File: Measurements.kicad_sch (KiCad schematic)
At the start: 23 parts, among them U5 LMV324

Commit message: Первая версия в производство
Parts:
- added J12: Current Measure, Connector_Molex:Molex_Micro-Fit_3.0_43045-0400_2x02_P3.00mm_Horizontal, symbol Connector_Generic:Conn_02x02_Odd_Even
- added J6: Voltage measure, Connector_Molex:Molex_Micro-Fit_3.0_43045-0400_2x02_P3.00mm_Horizontal, symbol Connector_Generic:Conn_02x02_Odd_Even
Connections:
- net GND: now also J12.1 (Pin_1), J12.3 (Pin_3), J6.1 (Pin_1), J6.2 (Pin_2)
- net I_INDUCT: now also J12.2 (Pin_2), J12.4 (Pin_4)
- net V_IN: now also J6.3 (Pin_3)
- net V_OUT: now also J6.4 (Pin_4)
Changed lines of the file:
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@@
   (junction (at 133.985 68.58) (diameter 0) (color 0 0 0 0)
+  )
+  (junction (at 73.66 114.554) (diameter 0) (color 0 0 0 0)
   )
   (junction (at 144.145 68.58) (diameter 0) (color 0 0 0 0)
@@
   (no_connect (at 148.59 53.34))
   (no_connect (at 148.59 48.26))
+  (wire (pts (xy 72.39 112.014) (xy 73.66 112.014))
+    (stroke (width 0) (type default) (color 0 0 0 0))
+  )
   (wire (pts (xy 175.26 71.12) (xy 177.165 71.12))
     (stroke (width 0) (type default) (color 0 0 0 0))
@@
     (stroke (width 0) (type default) (color 0 0 0 0))
   )
+  (wire (pts (xy 56.896 112.014) (xy 56.896 114.554))
+    (stroke (width 0) (type default) (color 0 0 0 0))
+  )
   (wire (pts (xy 133.985 68.58) (xy 133.985 70.485))
     (stroke (width 0) (type default) (color 0 0 0 0))
   )
+  (wire (pts (xy 72.39 114.554) (xy 73.66 114.554))
+    (stroke (width 0) (type default) (color 0 0 0 0))
+  )
+  (wire (pts (xy 73.66 112.014) (xy 73.66 114.554))
+    (stroke (width 0) (type default) (color 0 0 0 0))
+  )
   (wire (pts (xy 211.455 95.885) (xy 211.455 96.52))
     (stroke (width 0) (type default) (color 0 0 0 0))
@@
     (stroke (width 0) (type default) (color 0 0 0 0))
   )
+  (wire (pts (xy 55.88 130.556) (xy 55.88 131.318))
+    (stroke (width 0) (type default) (color 0 0 0 0))
+  )
   (wire (pts (xy 143.51 100.33) (xy 143.51 99.695))
     (stroke (width 0) (type default) (color 0 0 0 0))
@@
     (stroke (width 0) (type default) (color 0 0 0 0))
   )
+  (wire (pts (xy 55.88 131.318) (xy 59.69 131.318))
+    (stroke (width 0) (type default) (color 0 0 0 0))
+  )
   (wire (pts (xy 133.985 68.58) (xy 135.89 68.58))
     (stroke (width 0) (type default) (color 0 0 0 0))
@@
     (stroke (width 0) (type default) (color 0 0 0 0))
   )
+  (wire (pts (xy 76.2 131.318) (xy 76.2 130.556))
+    (stroke (width 0) (type default) (color 0 0 0 0))
+  )
   (wire (pts (xy 143.51 117.475) (xy 143.51 118.745))
     (stroke (width 0) (type default) (color 0 0 0 0))
@@
     (stroke (width 0) (type default) (color 0 0 0 0))
   )
+  (wire (pts (xy 59.69 114.554) (xy 56.896 114.554))
+    (stroke (width 0) (type default) (color 0 0 0 0))
+  )
   (wire (pts (xy 140.97 68.58) (xy 144.145 68.58))
     (stroke (width 0) (type default) (color 0 0 0 0))
@@
     (stroke (width 0) (type default) (color 0 0 0 0))
   )
+  (wire (pts (xy 73.66 114.554) (xy 73.66 115.57))
+    (stroke (width 0) (type default) (color 0 0 0 0))
+  )
   (wire (pts (xy 143.51 124.46) (xy 143.51 123.825))
     (stroke (width 0) (type default) (color 0 0 0 0))
@@
     (stroke (width 0) (type default) (color 0 0 0 0))
   )
+  (wire (pts (xy 76.2 131.318) (xy 72.39 131.318))
+    (stroke (width 0) (type default) (color 0 0 0 0))
+  )
   (wire (pts (xy 127 120.015) (xy 127 124.46))
     (stroke (width 0) (type default) (color 0 0 0 0))
@@
     (stroke (width 0) (type default) (color 0 0 0 0))
   )
+  (wire (pts (xy 59.69 112.014) (xy 56.896 112.014))
+    (stroke (width 0) (type default) (color 0 0 0 0))
+  )
   (wire (pts (xy 174.625 120.015) (xy 176.53 120.015))
     (stroke (width 0) (type default) (color 0 0 0 0))
+  )
+  (global_label "V_OUT" (shape input) (at 72.39 133.858 0) (fields_autoplaced)
+    (effects (font (size 1.27 1.27)) (justify left))
+    (property "Intersheet References" "${INTERSHEET_REFS}" (id 0) (at 80.4879 133.9374 0)
+      (effects (font (size 1.27 1.27)) (justify left) hide)
+    )
   )
   (global_label "I_INDUCT" (shape input) (at 127 110.49 180) (fields_autoplaced)
@@
     )
   )
+  (global_label "V_IN" (shape input) (at 59.69 133.858 180) (fields_autoplaced)
+    (effects (font (size 1.27 1.27)) (justify right))
+    (property "Intersheet References" "${INTERSHEET_REFS}" (id 0) (at 53.2855 133.7786 0)
+      (effects (font (size 1.27 1.27)) (justify right) hide)
+    )
+  )
   (global_label "V_OUT_ADC" (shape input) (at 177.165 95.885 0) (fields_autoplaced)
     (effects (font (size 1.27 1.27)) (justify left))
@@
     (effects (font (size 1.27 1.27)) (justify right))
     (property "Intersheet References" "${INTERSHEET_REFS}" (id 0) (at 121.2305 61.5156 0)
+      (effects (font (size 1.27 1.27)) (justify right) hide)
+    )
+  )
+  (global_label "I_INDUCT" (shape input) (at 56.896 113.284 180) (fields_autoplaced)
+    (effects (font (size 1.27 1.27)) (justify right))
+    (property "Intersheet References" "${INTERSHEET_REFS}" (id 0) (at 46.1372 113.2046 0)
       (effects (font (size 1.27 1.27)) (justify right) hide)
     )
@@
     (pin "2")
   )
+  (symbol (lib_id "power:GND") (at 55.88 130.556 180) (unit 1)
+    (in_bom yes) (on_board yes)
+    (property "Reference" "#PWR027" (id 0) (at 55.88 124.206 0)
+      (effects (font (size 1.27 1.27)) hide)
+    )
+    (property "Value" "GND" (id 1) (at 55.88 127 0))
+    (property "Footprint" "" (id 2) (at 55.88 130.556 0)
+      (effects (font (size 1.27 1.27)) hide)
+    )
+    (property "Datasheet" "" (id 3) (at 55.88 130.556 0)
+      (effects (font (size 1.27 1.27)) hide)
+    )
+    (pin "1")
+  )
+  (symbol (lib_id "power:GND") (at 73.66 115.57 0) (unit 1)
+    (in_bom yes) (on_board yes)
+    (property "Reference" "#PWR028" (id 0) (at 73.66 121.92 0)
+      (effects (font (size 1.27 1.27)) hide)
+    )
+    (property "Value" "GND" (id 1) (at 75.438 119.126 0)
+      (effects (font (size 1.27 1.27)) (justify right))
+    )
+    (property "Footprint" "" (id 2) (at 73.66 115.57 0)
+      (effects (font (size 1.27 1.27)) hide)
+    )
+    (property "Datasheet" "" (id 3) (at 73.66 115.57 0)
+      (effects (font (size 1.27 1.27)) hide)
+    )
+    (pin "1")
+  )
   (symbol (lib_id "Device:R_Small") (at 133.35 97.79 180) (unit 1)
     (in_bom yes) (on_board yes)
@@
     )
     (pin "1")
+  )
+  (symbol (lib_id "Connector_Generic:Conn_02x02_Odd_Even") (at 67.31 114.554 180) (unit 1)
+    (in_bom yes) (on_board yes) (fields_autoplaced)
+    (property "Reference" "J12" (id 0) (at 66.04 105.41 0))
+    (property "Value" "Current Measure" (id 1) (at 66.04 107.95 0))
+    (property "Footprint" "Connector_Molex:Molex_Micro-Fit_3.0_43045-0400_2x02_P3.00mm_Horizontal" (id 2) (at 67.31 114.554 0)
+      (effects (font (size 1.27 1.27)) hide)
+    )
+    (property "Datasheet" "~" (id 3) (at 67.31 114.554 0)
+      (effects (font (size 1.27 1.27)) hide)
+    )
+    (pin "1")
+    (pin "2")
+    (pin "3")
+    (pin "4")
   )
   (symbol (lib_id "Device:R_Small") (at 167.005 120.015 270) (unit 1)
@@
     (pin "2")
   )
+  (symbol (lib_id "Connector_Generic:Conn_02x02_Odd_Even") (at 64.77 131.318 0) (unit 1)
+    (in_bom yes) (on_board yes) (fields_autoplaced)
+    (property "Reference" "J6" (id 0) (at 66.04 125.222 0))
+    (property "Value" "Voltage measure" (id 1) (at 66.04 127.762 0))
+    (property "Footprint" "Connector_Molex:Molex_Micro-Fit_3.0_43045-0400_2x02_P3.00mm_Horizontal" (id 2) (at 64.77 131.318 0)
+      (effects (font (size 1.27 1.27)) hide)
+    )
+    (property "Datasheet" "~" (id 3) (at 64.77 131.318 0)
+      (effects (font (size 1.27 1.27)) hide)
+    )
+    (pin "1")
+    (pin "2")
+    (pin "3")
+    (pin "4")
+  )
   (symbol (lib_id "Device:C_Small") (at 127.635 68.58 0) (unit 1)
     (in_bom yes) (on_board yes)
@@
     (pin "2")
   )
+  (symbol (lib_id "power:GND") (at 76.2 130.556 180) (unit 1)
+    (in_bom yes) (on_board yes)
+    (property "Reference" "#PWR029" (id 0) (at 76.2 124.206 0)
+      (effects (font (size 1.27 1.27)) hide)
+    )
+    (property "Value" "GND" (id 1) (at 74.422 127 0)
+      (effects (font (size 1.27 1.27)) (justify right))
+    )
+    (property "Footprint" "" (id 2) (at 76.2 130.556 0)
+      (effects (font (size 1.27 1.27)) hide)
+    )
+    (property "Datasheet" "" (id 3) (at 76.2 130.556 0)
+      (effects (font (size 1.27 1.27)) hide)
+    )
+    (pin "1")
+  )
   (symbol (lib_id "Device:R_Small") (at 133.985 64.135 180) (unit 1)

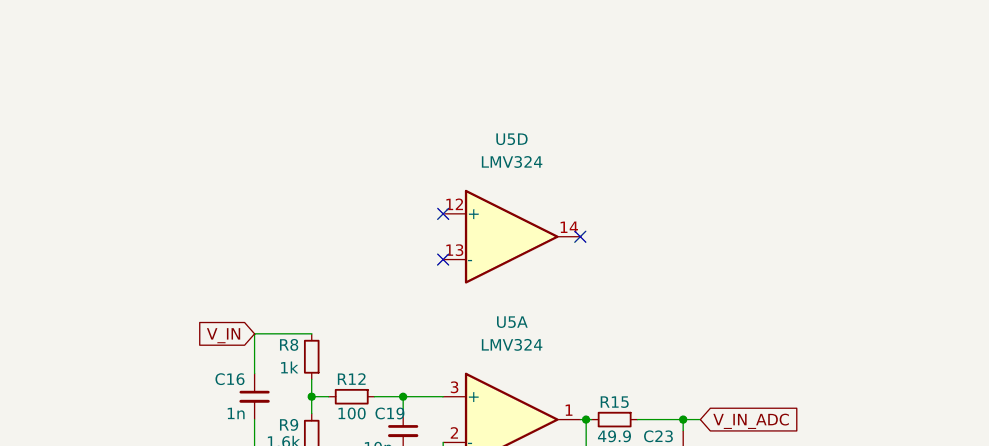
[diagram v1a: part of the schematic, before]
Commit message: Добавил температуру, убрал подтяжки RS-485, заменил ШИМ на дифференциальный сигнал, добавил земли RS-485
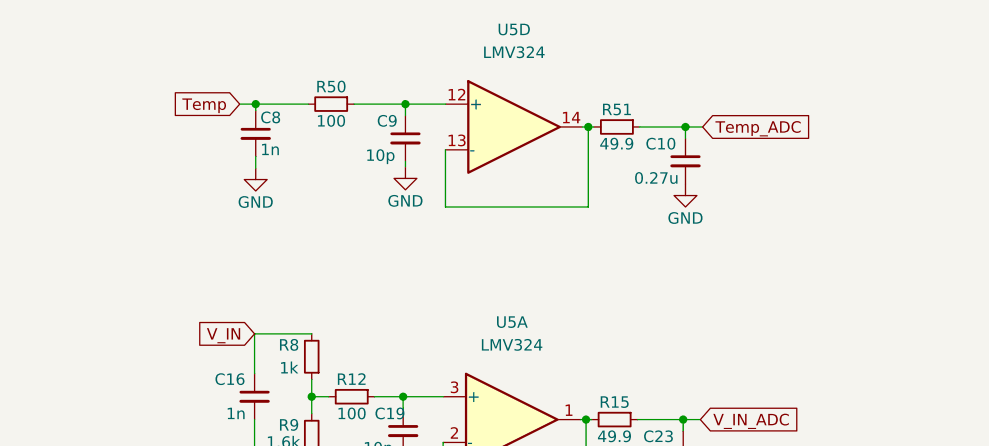
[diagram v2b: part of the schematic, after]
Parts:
- added C10: 0.27u, Capacitor_SMD:C_0805_2012Metric_Pad1.18x1.45mm_HandSolder, symbol Device:C_Small
- added C8: 1n, Capacitor_SMD:C_0805_2012Metric_Pad1.18x1.45mm_HandSolder, symbol Device:C_Small
- added C9: 10p, Capacitor_SMD:C_0805_2012Metric_Pad1.18x1.45mm_HandSolder, symbol Device:C_Small
- added R50: 100, Resistor_SMD:R_0805_2012Metric_Pad1.20x1.40mm_HandSolder, symbol Device:R_Small
- added R51: 49.9, Resistor_SMD:R_0805_2012Metric_Pad1.20x1.40mm_HandSolder, symbol Device:R_Small
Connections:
- net GND: now also C10.2, C8.2, C9.2
- net at U5.12 (+): now also C9.1, R50.1
- net at U5.13 (-): now also U5.14, R51.2
- new net Temp: C8.1, R50.2
- new net Temp_ADC: C10.1, R51.1
- no-connect marks 3 -> 0
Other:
- moved on the sheet: U5D
